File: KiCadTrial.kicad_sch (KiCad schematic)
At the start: 3 parts, among them J1 Conn_01x02

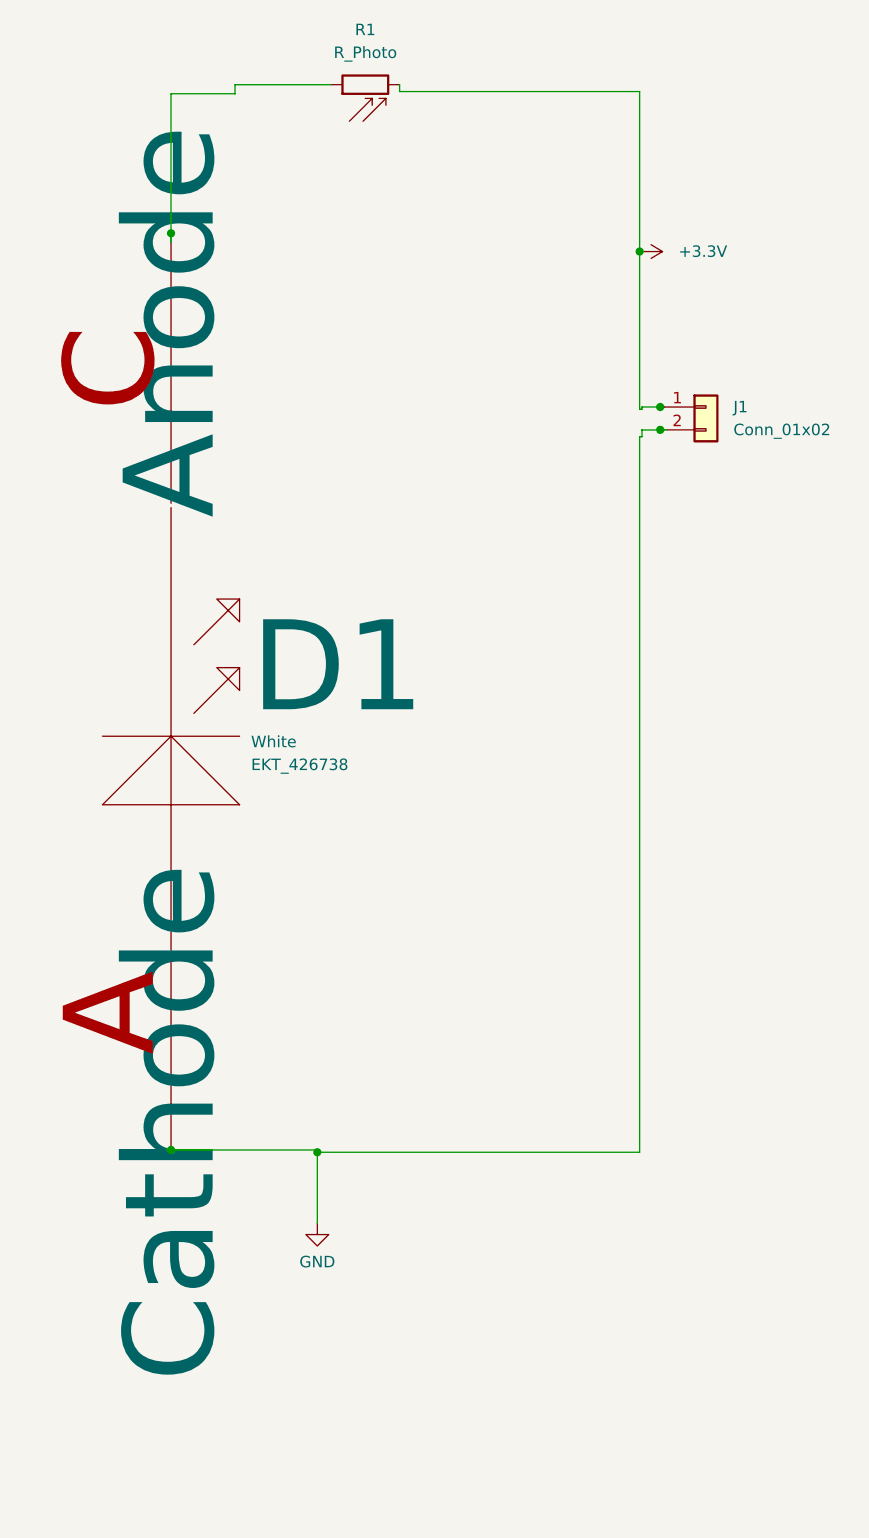
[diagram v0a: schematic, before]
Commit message: JLCPCB PN
added JLCPCB PN to all components.
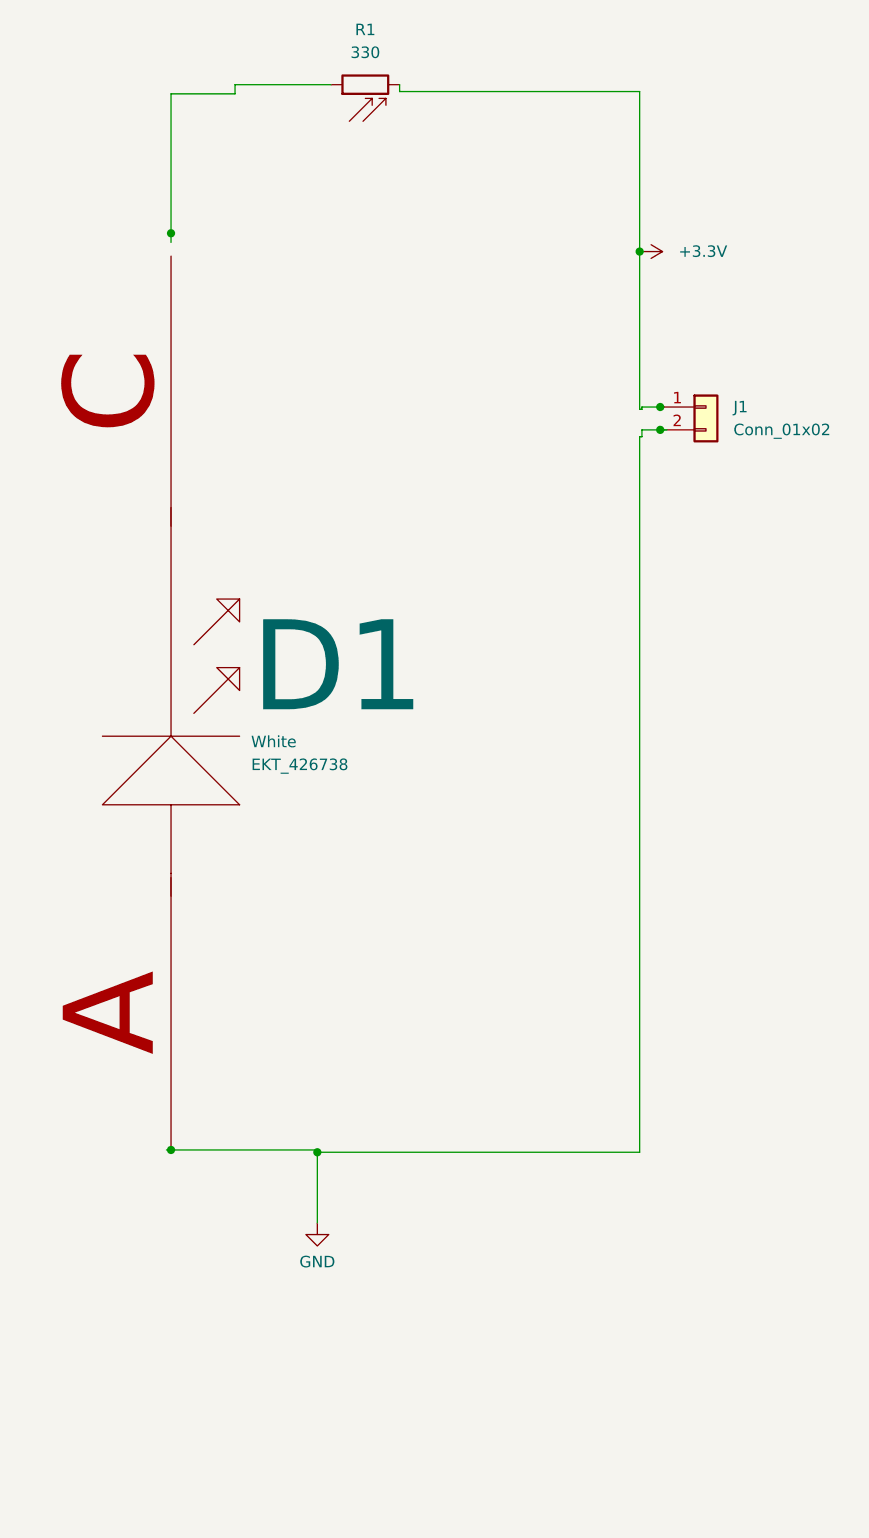
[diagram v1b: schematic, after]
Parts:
- D1: JLCPCB (none) -> C965805; MPN (none) -> XL-1608SYGC-06; Manufacturer (none) -> XINGLIGHT
- J1: JLCPCB (none) -> C5116481; MPN (none) -> 2.54-1*2; Manufacturer (none) -> ZHOURI; PN (none) -> anything
- R1: value R_Photo -> 330; JLCPCB (none) -> C23138; MPN (none) -> 0603WAF3300T5E; Manufacturer (none) -> UNI-ROYAL(Uniroyal Elec); PN (none) -> something
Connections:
- net at D1.C (Cathode): no longer R1.1
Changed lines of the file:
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@@
       (effects (font (size 1.27 1.27)) (justify left))
+    )
+    (property "JLCPCB" "C965805" (at 104.14 109.22 0)
+      (effects (font (size 1.27 1.27)) hide)
+    )
+    (property "MPN" "XL-1608SYGC-06" (at 104.14 109.22 0)
+      (effects (font (size 1.27 1.27)) hide)
+    )
+    (property "Manufacturer" "XINGLIGHT" (at 104.14 109.22 0)
+      (effects (font (size 1.27 1.27)) hide)
     )
     (pin "C")
@@
       (effects (font (size 1.27 1.27)))
     )
-    (property "Value" "R_Photo" (at 125.73 38.354 90)
+    (property "Value" "330" (at 125.73 38.354 90)
       (effects (font (size 1.27 1.27)))
     )
@@
     )
     (property "Datasheet" "~" (at 127 41.91 0)
+      (effects (font (size 1.27 1.27)) hide)
+    )
+    (property "PN" "something" (at 125.73 41.91 0)
+      (effects (font (size 1.27 1.27)) hide)
+    )
+    (property "JLCPCB" "C23138" (at 125.73 41.91 0)
+      (effects (font (size 1.27 1.27)) hide)
+    )
+    (property "MPN" "0603WAF3300T5E" (at 125.73 41.91 0)
+      (effects (font (size 1.27 1.27)) hide)
+    )
+    (property "Manufacturer" "UNI-ROYAL(Uniroyal Elec)" (at 125.73 41.91 0)
       (effects (font (size 1.27 1.27)) hide)
     )
@@
       (effects (font (size 1.27 1.27)) hide)
     )
+    (property "PN" "anything" (at 163.576 77.724 0)
+      (effects (font (size 1.27 1.27)) hide)
+    )
+    (property "JLCPCB" "C5116481" (at 163.576 77.724 0)
+      (effects (font (size 1.27 1.27)) hide)
+    )
+    (property "MPN" "2.54-1*2" (at 163.576 77.724 0)
+      (effects (font (size 1.27 1.27)) hide)
+    )
+    (property "Manufacturer" "ZHOURI" (at 163.576 77.724 0)
+      (effects (font (size 1.27 1.27)) hide)
+    )

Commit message: Design for manufacture
Added board description, version, and a space/place for the SN
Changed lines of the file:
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@@
     (comment 2 "Drawn by: NK")
-  )
-  (junction (at 104.14 58.42) (diameter 0) (color 0 0 0 0)
   )
   (junction (at 104.14 160.274) (diameter 0) (color 0 0 0 0)
@@
     (stroke (width 0) (type default))
   )
-  (wire (pts (xy 104.14 58.42) (xy 104.14 59.436))
+  (wire (pts (xy 104.14 42.926) (xy 104.14 59.436))
     (stroke (width 0) (type default))
   )
@@
     (stroke (width 0) (type default))
   )
-  (wire (pts (xy 104.14 42.926) (xy 104.14 58.42))
-    (stroke (width 0) (type default))
-  )

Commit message: Conn V2
numbered the pins of the connector on the bottom silkscreen layer
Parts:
- J1: footprint Connector_Molex:Molex_KK-254_AE-6410-02A_1x02_P2.54mm_Vertical -> myPCBLib:Molex_KK-254_AE-6410-02A_1x02_P2.54mm_Vertical
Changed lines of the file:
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@@
       (effects (font (size 1.27 1.27)) (justify left))
     )
-    (property "Footprint" "Connector_Molex:Molex_KK-254_AE-6410-02A_1x02_P2.54mm_Vertical" (at 163.576 77.724 0)
+    (property "Footprint" "myPCBLib:Molex_KK-254_AE-6410-02A_1x02_P2.54mm_Vertical" (at 163.576 77.724 0)
       (effects (font (size 1.27 1.27)) hide)
     )

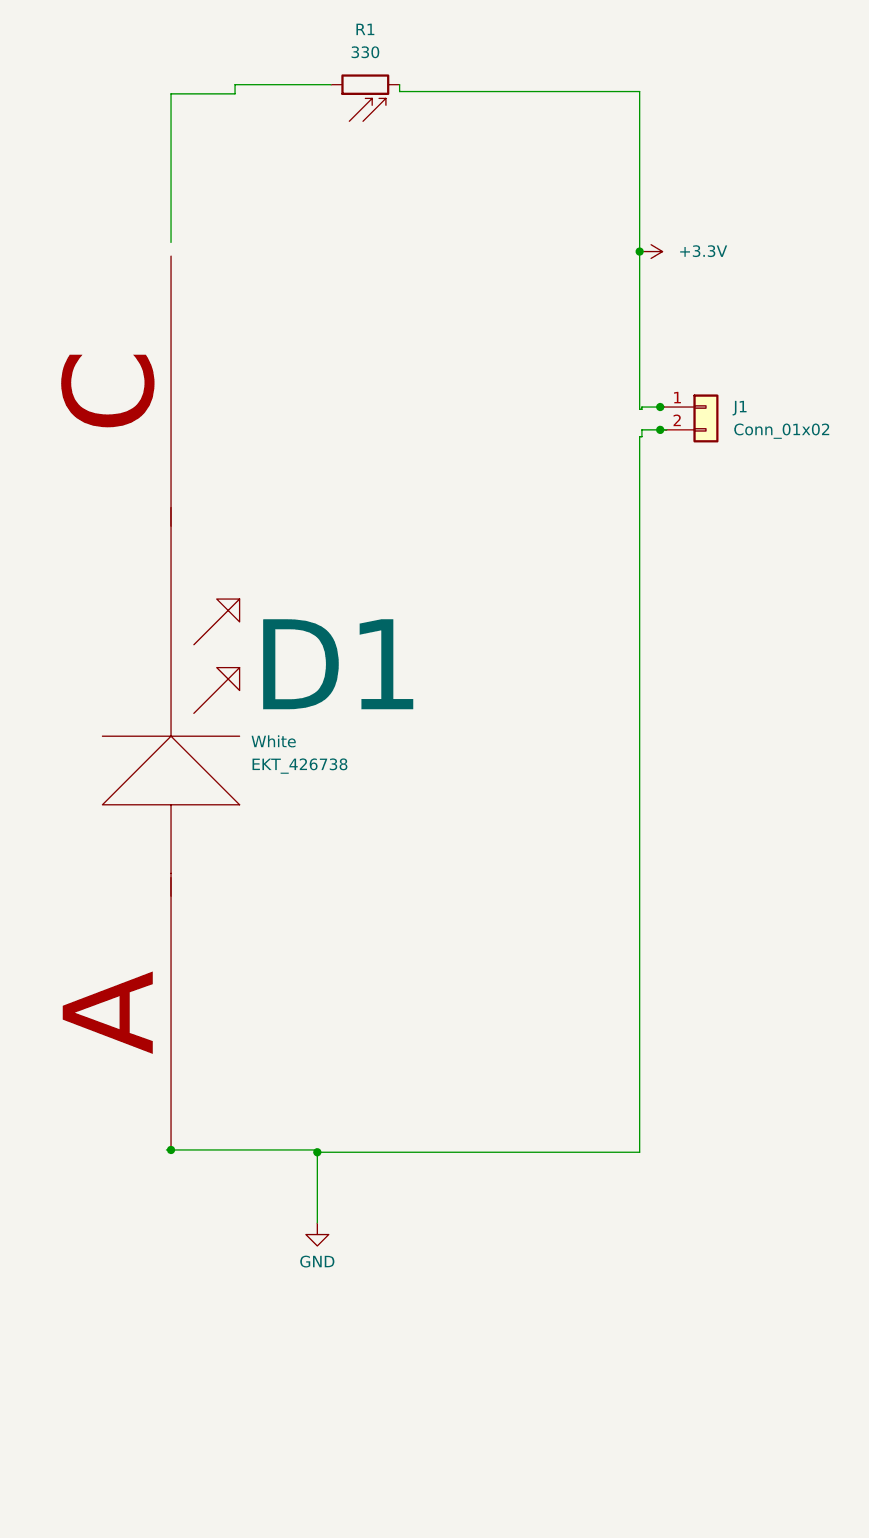
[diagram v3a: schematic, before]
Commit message: Led polarity correction
changed the polarity of the led connected between the resistor and the gnd
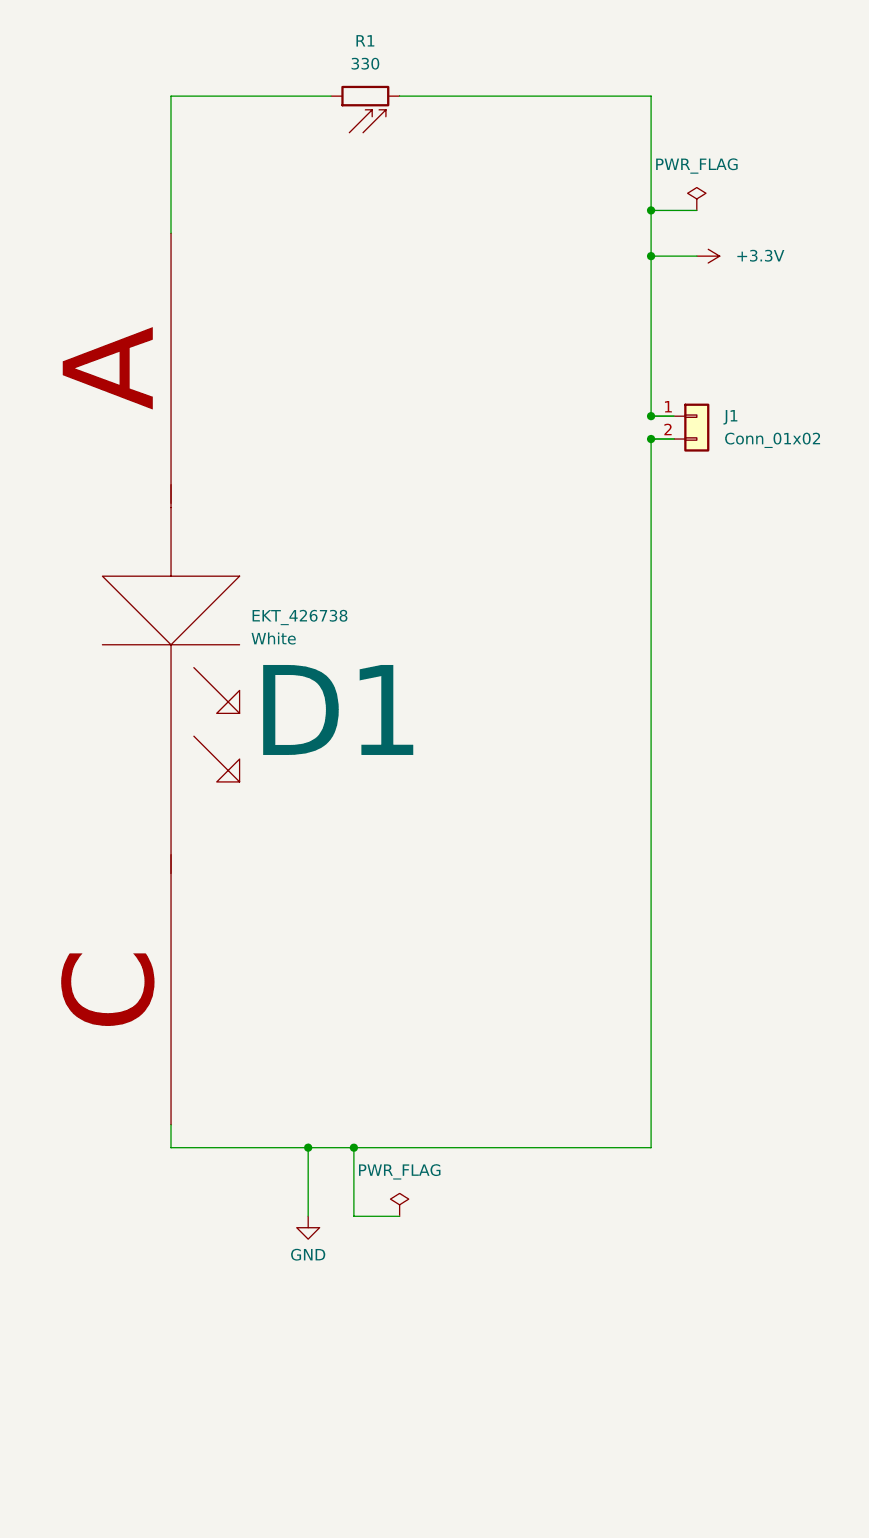
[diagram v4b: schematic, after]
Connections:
- net GND: now also D1.C (Cathode); no longer D1.A (Anode)
- net at R1.1: now also D1.A (Anode)
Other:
- moved on the sheet: D1, J1, R1
